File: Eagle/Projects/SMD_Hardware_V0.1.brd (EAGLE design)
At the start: 100 x 80 mm, 3 parts, among them IC1 LM386M-1

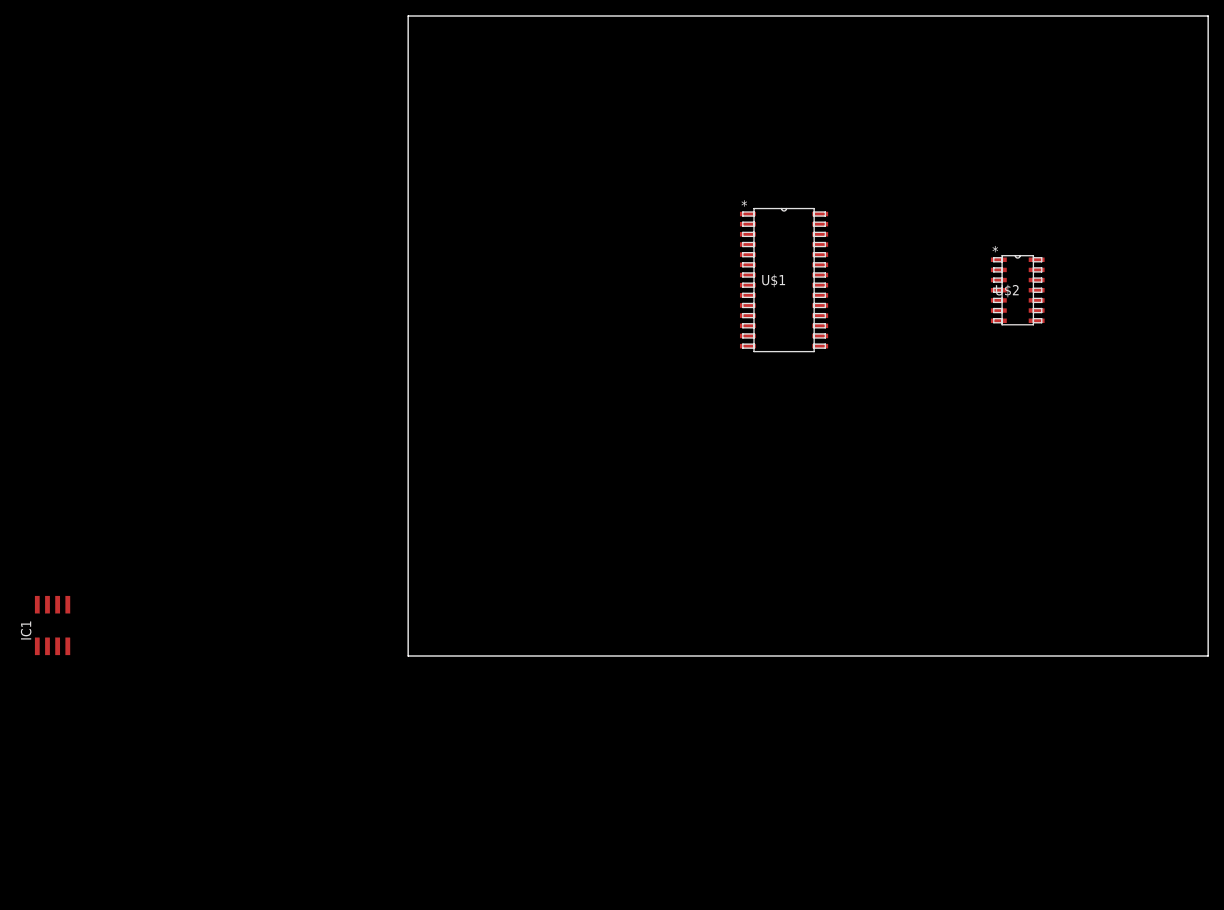
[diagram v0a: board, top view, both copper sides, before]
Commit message: Layed out the board a bit more, finished off some connections for the basic micro layout.  Need to add a power supply yet
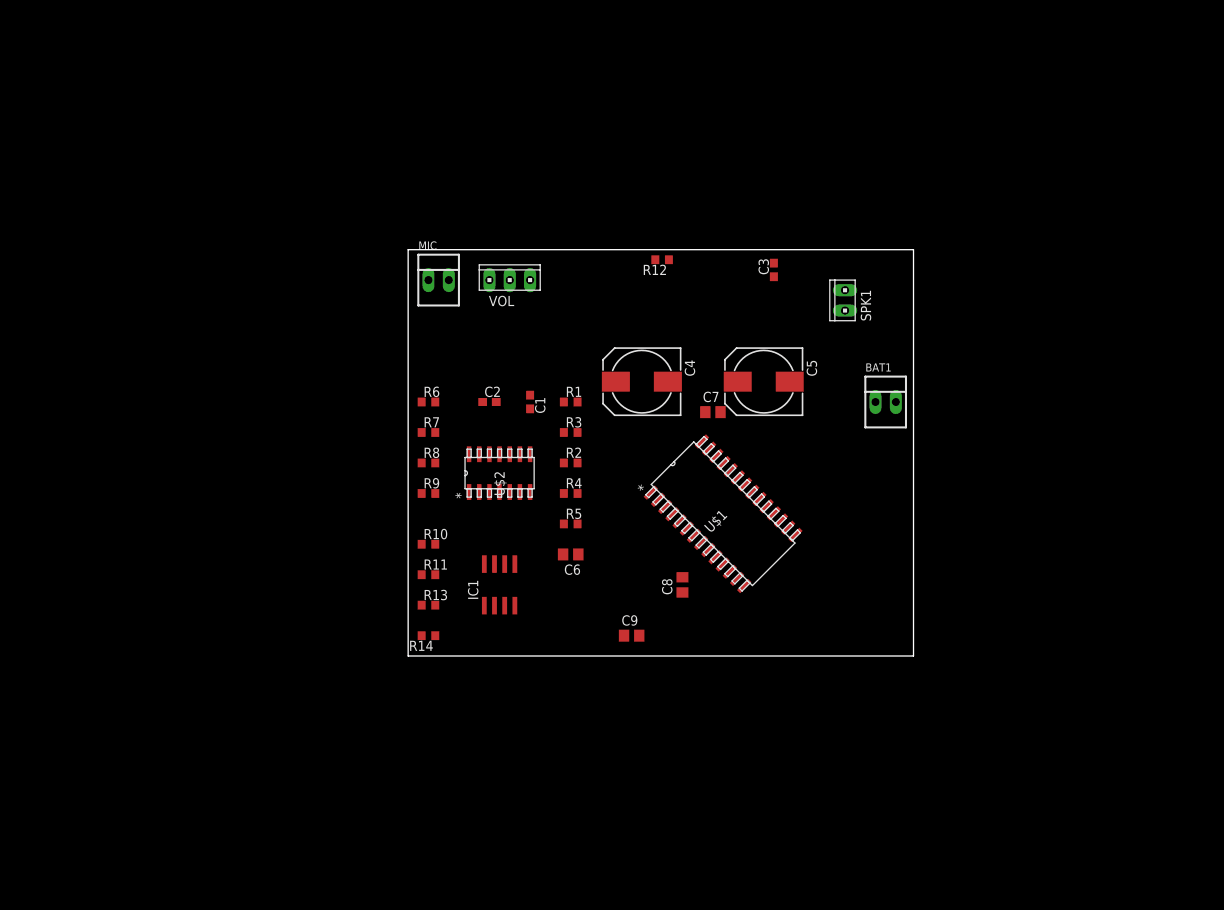
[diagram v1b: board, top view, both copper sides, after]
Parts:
- added BAT1, MIC: (no value), con-molex:22-23-2021
- added C1, C2, C3: (no value), resistor:C0603
- added C4, C5: (no value), resistor:140CLH-0810
- added C6, C7, C8, C9: (no value), resistor:C0805
- added R1, R10, R11, R12, R13, R14, R2, R3, R4, R5, R6, R7, R8, R9: (no value), resistor:R0603
- added SPK1: (no value), con-amp:10X02MTA
- added VOL: (no value), con-amp:10X03MTA
- moved U$2 68.7 mm to (11.4, 22.9), turned to 90 degrees
- moved IC1 56.1 mm to (11.4, 8.89)
- moved U$1 30.2 mm to (39.4, 17.8), turned to 45 degrees
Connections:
- removed net AVDD: U$1.28
- removed net AVSS: U$1.27
- removed net VCAP/VDDCORE: U$1.20
- removed net VS: IC1.6
- removed net VSS: U$1.19
- removed net VSS_2: U$1.8
- new net N$1: C1.1, MIC.1, R1.1
- new net N$10: R7.1, R9.2, U$2.12
- new net N$11: R6.2, U$1.23
- new net N$12: C4.-, U$1.2
- new net N$13: BAT1.2, IC1.6
- new net N$14: C2.2, VOL.1
- new net N$15: C3.2, C5.+, IC1.5
- new net N$16: C3.1, R12.2
- new net N$17: C5.-, SPK1.1
- new net N$18: C6.1, U$1.20
- new net N$19: C8.1, U$1.13
- new net N$2: C1.2, R2.1
- new net N$20: C8.2, U$1.19, U$1.8
- new net N$21: C7.1, U$1.28
- new net N$22: C7.2, U$1.27
- new net N$23: C9.1, R13.1, R14.2
- new net N$24: R14.1, U$1.1
- new net N$25: IC1.3, VOL.2
- new net N$3: R2.2, R3.1, U$2.2
- new net N$4: R4.2, R5.1, U$2.3
- new net N$5: R10.1, R11.2, R9.1
- new net N$6: C4.+, R3.2, U$2.1
- new net N$7: C2.1, R8.1, U$2.14
- new net N$8: R6.1, R8.2, U$2.13
- new net N$9: R7.2, U$1.24
- net GND: now also BAT1.1, C6.2, C9.2, IC1.2, MIC.2, R11.1, R12.1, R4.1, SPK1.2, U$2.11, VOL.3
- net VDD: now also R1.2, R10.2, R13.2, R5.2, U$2.4; no longer U$1.13
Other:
- board size 100 x 80 mm -> 63.2 x 50.8 mm

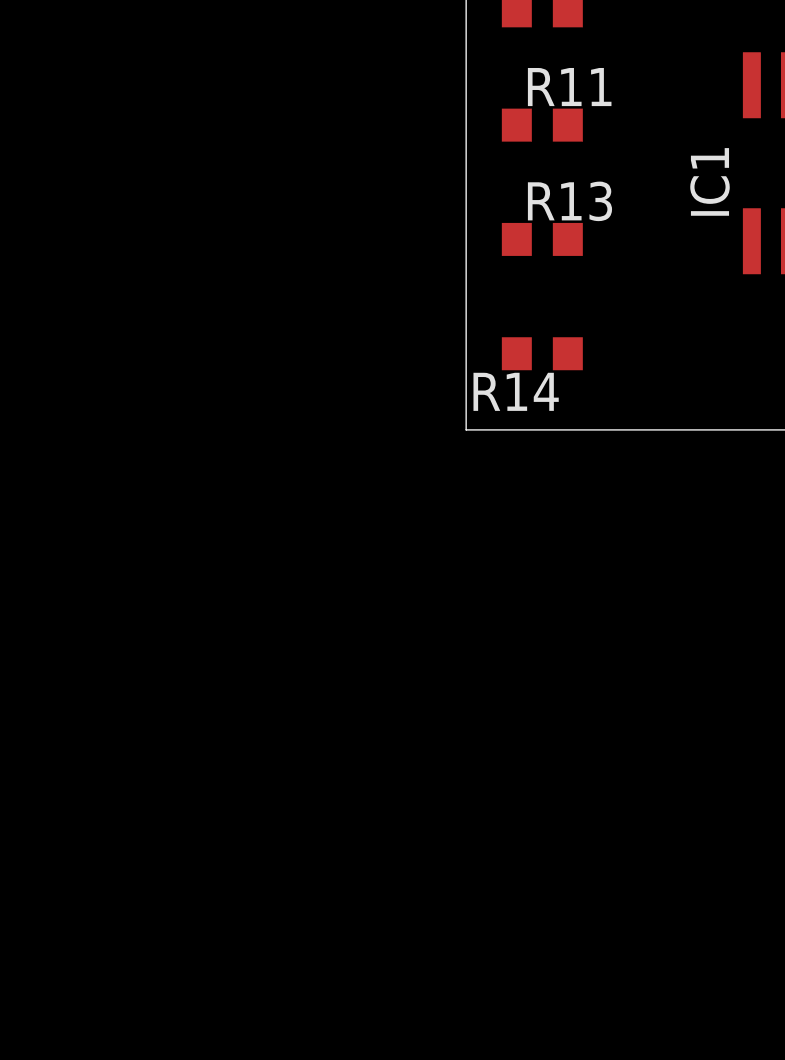
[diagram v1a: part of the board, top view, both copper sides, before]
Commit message: Started editing the eagle files with values from the breadboard, and was working on the code a bit more
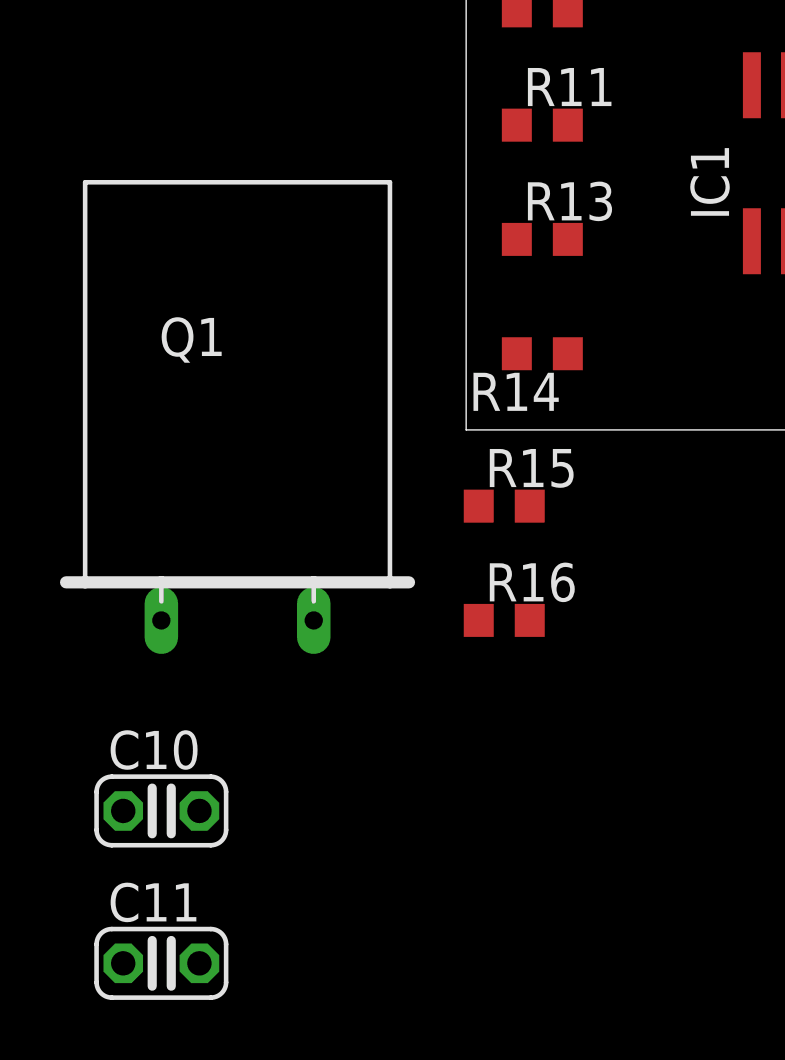
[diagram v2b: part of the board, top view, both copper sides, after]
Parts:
- added C10, C11: 10pF, resistor:C025-024X044
- added Q1: 12 MHz (ATS12A), special:Q
- added R15, R16: 1k, resistor:R0603
- C1: value (none) -> .1uF
- C4: value (none) -> .1uF 400V
- C5: value (none) -> 220uF 25V
- R1, R10, R11, R4, R5, R6, R7, R9: value (none) -> 10k
- R12: value (none) -> 10
- R2: value (none) -> 1k
- R3: value (none) -> 100k
- R8: value (none) -> Rheostat
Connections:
- removed net N$6: C4.+, R3.2, U$2.1
- new net N$26: C4.+, R15.1, R16.2, R3.2, U$2.1
- new net N$28: C11.1, Q1.1, U$1.9
- new net N$29: C10.1, Q1.2, U$1.10
- net GND: now also C10.2, C11.2, R15.2
- net VDD: now also R16.1
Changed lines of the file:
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@@
 <?xml version="1.0" encoding="utf-8"?>
 <!DOCTYPE eagle SYSTEM "eagle.dtd">
-<eagle version="7.3.0">
+<eagle version="7.6.0">
 <drawing>
 <settings>
@@
 <attribute name="OC_NEWARK" value="25C3832" x="3.81" y="46.99" size="1.778" layer="27" display="off"/>
 </element>
-<element name="C1" library="resistor" package="C0603" value="" x="15.24" y="31.75" rot="R270"/>
+<element name="C1" library="resistor" package="C0603" value=".1uF" x="15.24" y="31.75" rot="R270"/>
 <element name="C2" library="resistor" package="C0603" value="" x="10.16" y="31.75"/>
-<element name="R1" library="resistor" package="R0603" value="" x="20.32" y="31.75"/>
-<element name="R2" library="resistor" package="R0603" value="" x="20.32" y="24.13"/>
-<element name="R3" library="resistor" package="R0603" value="" x="20.32" y="27.94"/>
-<element name="R4" library="resistor" package="R0603" value="" x="20.32" y="20.32"/>
-<element name="R5" library="resistor" package="R0603" value="" x="20.32" y="16.51"/>
-<element name="R6" library="resistor" package="R0603" value="" x="2.54" y="31.75"/>
-<element name="R7" library="resistor" package="R0603" value="" x="2.54" y="27.94"/>
-<element name="R8" library="resistor" package="R0603" value="" x="2.54" y="24.13"/>
-<element name="R9" library="resistor" package="R0603" value="" x="2.54" y="20.32"/>
-<element name="R10" library="resistor" package="R0603" value="" x="2.54" y="13.97"/>
-<element name="R11" library="resistor" package="R0603" value="" x="2.54" y="10.16"/>
-<element name="C4" library="resistor" package="140CLH-0810" value="" x="29.21" y="34.29" rot="R180"/>
+<element name="R1" library="resistor" package="R0603" value="10k" x="20.32" y="31.75"/>
+<element name="R2" library="resistor" package="R0603" value="1k" x="20.32" y="24.13"/>
+<element name="R3" library="resistor" package="R0603" value="100k" x="20.32" y="27.94"/>
+<element name="R4" library="resistor" package="R0603" value="10k" x="20.32" y="20.32"/>
+<element name="R5" library="resistor" package="R0603" value="10k" x="20.32" y="16.51"/>
+<element name="R6" library="resistor" package="R0603" value="10k" x="2.54" y="31.75"/>
+<element name="R7" library="resistor" package="R0603" value="10k" x="2.54" y="27.94"/>
+<element name="R8" library="resistor" package="R0603" value="Rheostat" x="2.54" y="24.13"/>
+<element name="R9" library="resistor" package="R0603" value="10k" x="2.54" y="20.32"/>
+<element name="R10" library="resistor" package="R0603" value="10k" x="2.54" y="13.97"/>
+<element name="R11" library="resistor" package="R0603" value="10k" x="2.54" y="10.16"/>
+<element name="C4" library="resistor" package="140CLH-0810" value=".1uF 400V" x="29.21" y="34.29" rot="R180"/>
 <element name="BAT1" library="con-molex" package="22-23-2021" value="" x="59.69" y="31.75">
 <attribute name="MF" value="MOLEX" x="59.69" y="31.75" size="1.778" layer="27" display="off"/>
@@
 </element>
 <element name="C3" library="resistor" package="C0603" value="" x="45.72" y="48.26" rot="R90"/>
-<element name="C5" library="resistor" package="140CLH-0810" value="" x="44.45" y="34.29" rot="R180"/>
-<element name="R12" library="resistor" package="R0603" value="" x="31.75" y="49.53" rot="R180"/>
+<element name="C5" library="resistor" package="140CLH-0810" value="220uF 25V" x="44.45" y="34.29" rot="R180"/>
+<element name="R12" library="resistor" package="R0603" value="10" x="31.75" y="49.53" rot="R180"/>
 <element name="VOL" library="con-amp" package="10X03MTA" value="" x="12.7" y="46.99"/>
 <element name="SPK1" library="con-amp" package="10X02MTA" value="" x="54.61" y="44.45" rot="R90"/>
@@
 <element name="R13" library="resistor" package="R0603" value="" x="2.54" y="6.35"/>
 <element name="R14" library="resistor" package="R0603" value="" x="2.54" y="2.54" rot="R180"/>
+<element name="R15" library="resistor" package="R0603" value="1k" x="1.27" y="-2.54"/>
+<element name="R16" library="resistor" package="R0603" value="1k" x="1.27" y="-6.35"/>
+<element name="Q1" library="special" package="Q" value="12 MHz (ATS12A)" x="-7.62" y="1.27"/>
+<element name="C10" library="resistor" package="C025-024X044" value="10pF" x="-10.16" y="-12.7"/>
+<element name="C11" library="resistor" package="C025-024X044" value="10pF" x="-10.16" y="-17.78"/>
 </elements>
 <signals>
@@
 <contactref element="R13" pad="2"/>
 <contactref element="R1" pad="2"/>
+<contactref element="R16" pad="1"/>
 <wire x1="11.43" y1="20.4978" x2="21.17" y2="31.75" width="0" layer="19" extent="1-1"/>
 <wire x1="3.39" y1="13.97" x2="11.43" y2="20.4978" width="0" layer="19" extent="1-1"/>
+<wire x1="3.39" y1="6.35" x2="3.39" y2="13.97" width="0" layer="19" extent="1-1"/>
 <wire x1="21.17" y1="16.51" x2="11.43" y2="20.4978" width="0" layer="19" extent="1-1"/>
-<wire x1="3.39" y1="6.35" x2="3.39" y2="13.97" width="0" layer="19" extent="1-1"/>
+<wire x1="0.42" y1="-6.35" x2="3.39" y2="6.35" width="0" layer="19" extent="1-1"/>
 </signal>
 <signal name="GND">
@@
 <contactref element="R12" pad="1"/>
 <contactref element="SPK1" pad="2"/>
+<contactref element="R15" pad="2"/>
+<contactref element="C11" pad="2"/>
+<contactref element="C10" pad="2"/>
 <wire x1="58.42" y1="31.75" x2="54.61" y2="43.18" width="0" layer="19" extent="1-1"/>
-<wire x1="1.69" y1="10.16" x2="58.42" y2="31.75" width="0" layer="19" extent="1-1"/>
 <wire x1="32.6" y1="49.53" x2="54.61" y2="43.18" width="0" layer="19" extent="1-1"/>
-<wire x1="10.795" y1="6.29" x2="32.6" y2="49.53" width="0" layer="19" extent="1-1"/>
-<wire x1="13.335" y1="6.29" x2="10.795" y2="6.29" width="0" layer="19" extent="1-1"/>
-<wire x1="10.16" y1="46.99" x2="10.795" y2="6.29" width="0" layer="19" extent="1-1"/>
+<wire x1="10.16" y1="46.99" x2="32.6" y2="49.53" width="0" layer="19" extent="1-1"/>
 <wire x1="5.08" y1="46.99" x2="10.16" y2="46.99" width="0" layer="19" extent="1-1"/>
-<wire x1="11.43" y1="25.2222" x2="13.335" y2="6.29" width="0" layer="19" extent="1-1"/>
+<wire x1="11.43" y1="25.2222" x2="10.16" y2="46.99" width="0" layer="19" extent="1-1"/>
 <wire x1="19.47" y1="20.32" x2="11.43" y2="25.2222" width="0" layer="19" extent="1-1"/>
 <wire x1="19.37" y1="12.7" x2="19.47" y2="20.32" width="0" layer="19" extent="1-1"/>
+<wire x1="13.335" y1="6.29" x2="19.37" y2="12.7" width="0" layer="19" extent="1-1"/>
+<wire x1="10.795" y1="6.29" x2="13.335" y2="6.29" width="0" layer="19" extent="1-1"/>
+<wire x1="1.69" y1="10.16" x2="10.795" y2="6.29" width="0" layer="19" extent="1-1"/>
+<wire x1="2.12" y1="-2.54" x2="10.795" y2="6.29" width="0" layer="19" extent="1-1"/>
 <wire x1="28.89" y1="2.54" x2="19.37" y2="12.7" width="0" layer="19" extent="1-1"/>
+<wire x1="-8.89" y1="-12.7" x2="2.12" y2="-2.54" width="0" layer="19" extent="1-1"/>
+<wire x1="-8.89" y1="-17.78" x2="-8.89" y2="-12.7" width="0" layer="19" extent="1-1"/>
 </signal>
 <signal name="N$1">
@@
 <wire x1="19.47" y1="16.51" x2="21.17" y2="20.32" width="0" layer="19" extent="1-1"/>
 </signal>
-<signal name="N$6">
-<contactref element="R3" pad="2"/>
-<contactref element="U$2" pad="1"/>
-<contactref element="C4" pad="+"/>
-<wire x1="21.17" y1="27.94" x2="7.62" y2="20.4978" width="0" layer="19" extent="1-1"/>
-<wire x1="25.96" y1="34.29" x2="21.17" y2="27.94" width="0" layer="19" extent="1-1"/>
-</signal>
 <signal name="N$5">
 <contactref element="R10" pad="1"/>
@@
 <wire x1="34.29" y1="9.84" x2="36.622040625" y2="14.134015625" width="0" layer="19" extent="1-1"/>
 </signal>
+<signal name="N$26">
+<contactref element="R16" pad="2"/>
+<contactref element="R15" pad="1"/>
+<contactref element="R3" pad="2"/>
+<contactref element="U$2" pad="1"/>
+<contactref element="C4" pad="+"/>
+<wire x1="21.17" y1="27.94" x2="25.96" y2="34.29" width="0" layer="19" extent="1-1"/>
+<wire x1="7.62" y1="20.4978" x2="21.17" y2="27.94" width="0" layer="19" extent="1-1"/>
+<wire x1="0.42" y1="-2.54" x2="7.62" y2="20.4978" width="0" layer="19" extent="1-1"/>
+<wire x1="2.12" y1="-6.35" x2="0.42" y2="-2.54" width="0" layer="19" extent="1-1"/>
+</signal>
+<signal name="N$28">
+<contactref element="C11" pad="1"/>
+<contactref element="Q1" pad="1"/>
+<contactref element="U$1" pad="9"/>
+<wire x1="-10.16" y1="-6.35" x2="37.520065625" y2="13.2359875" width="0" layer="19" extent="1-1"/>
+<wire x1="-11.43" y1="-17.78" x2="-10.16" y2="-6.35" width="0" layer="19" extent="1-1"/>
+</signal>
+<signal name="N$29">
+<contactref element="C10" pad="1"/>
+<contactref element="Q1" pad="2"/>
+<contactref element="U$1" pad="10"/>
+<wire x1="-5.08" y1="-6.35" x2="38.418090625" y2="12.3379625" width="0" layer="19" extent="1-1"/>
+<wire x1="-11.43" y1="-12.7" x2="-5.08" y2="-6.35" width="0" layer="19" extent="1-1"/>
+</signal>
 </signals>

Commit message: Eagle changes
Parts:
- C9: value (none) -> DNI
- R13: value (none) -> 10k
- R14: value (none) -> 0 (short)
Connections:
- new net N$27: U$1.4
- new net N$6: U$1.5
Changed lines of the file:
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@@
 <element name="C7" library="resistor" package="C0805" value="" x="38.1" y="30.48"/>
 <element name="C8" library="resistor" package="C0805" value="" x="34.29" y="8.89" rot="R90"/>
-<element name="C9" library="resistor" package="C0805" value="" x="27.94" y="2.54"/>
-<element name="R13" library="resistor" package="R0603" value="" x="2.54" y="6.35"/>
-<element name="R14" library="resistor" package="R0603" value="" x="2.54" y="2.54" rot="R180"/>
+<element name="C9" library="resistor" package="C0805" value="DNI" x="27.94" y="2.54"/>
+<element name="R13" library="resistor" package="R0603" value="10k" x="2.54" y="6.35"/>
+<element name="R14" library="resistor" package="R0603" value="0 (short)" x="2.54" y="2.54" rot="R180"/>
 <element name="R15" library="resistor" package="R0603" value="1k" x="1.27" y="-2.54"/>
 <element name="R16" library="resistor" package="R0603" value="1k" x="1.27" y="-6.35"/>
@@
 <wire x1="-11.43" y1="-12.7" x2="-5.08" y2="-6.35" width="0" layer="19" extent="1-1"/>
 </signal>
+<signal name="N$6">
+<contactref element="U$1" pad="5"/>
+</signal>
+<signal name="N$27">
+<contactref element="U$1" pad="4"/>
+</signal>
 </signals>
